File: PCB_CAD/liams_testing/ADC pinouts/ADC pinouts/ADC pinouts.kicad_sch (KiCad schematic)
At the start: 7 parts, among them U1 AK5720VT

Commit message: Changed some i2s configuation in stm32cubeMX, continued to update pinouts for the ADC
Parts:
- added J1: Conn_Coaxial_x2, symbol Connector:Conn_Coaxial_x2
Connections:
- net GND: now also J1.3 (EXT)
- net left channel in: no longer names the net of U1.3 (LIN)
- net left channel in: now also J1.2 (IN2)
- net right channel in: no longer names the net of U1.2 (RIN)
- net right channel in: now also J1.1 (IN1)
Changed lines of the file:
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@@
 		)
 	)
-	(label "right channel in"
-		(at 97.79 64.77 0)
+	(label "to ucontroller"
+		(at 144.78 64.77 0)
 		(fields_autoplaced yes)
 		(effects
@@
 	)
 	(label "to ucontroller"
-		(at 144.78 64.77 0)
+		(at 144.78 62.23 0)
 		(fields_autoplaced yes)
 		(effects
@@
 		)
 	)
-	(label "to ucontroller"
-		(at 144.78 62.23 0)
+	(label "data line to microcontroller"
+		(at 158.75 69.85 0)
 		(fields_autoplaced yes)
 		(effects
@@
 		)
 	)
-	(label "left channel in"
-		(at 97.79 69.85 0)
-		(fields_autoplaced yes)
-		(effects
-			(font
-				(size 1.27 1.27)
-			)
-			(justify left bottom)
-		)
-	)
-	(label "data line to microcontroller"
-		(at 158.75 69.85 0)
-		(fields_autoplaced yes)
-		(effects
-			(font
-				(size 1.27 1.27)
-			)
-			(justify left bottom)
+	(symbol
+		(lib_id "Connector:Conn_Coaxial_x2")
+		(at 92.71 67.31 0)
+		(mirror y)
+		(unit 1)
+		(exclude_from_sim no)
+		(in_bom yes)
+		(on_board yes)
+		(dnp no)
+		(property "Reference" "J1"
+			(at 88.9 66.3331 0)
+			(effects
+				(font
+					(size 1.27 1.27)
+				)
+				(justify left)
+			)
+		)
+		(property "Value" "Conn_Coaxial_x2"
+			(at 88.9 68.8731 0)
+			(effects
+				(font
+					(size 1.27 1.27)
+				)
+				(justify left)
+			)
+		)
+		(property "Footprint" ""
+			(at 92.71 69.85 0)
+			(effects
+				(font
+					(size 1.27 1.27)
+				)
+				(hide yes)
+			)
+		)
+		(property "Datasheet" "~"
+			(at 92.71 69.85 0)
+			(effects
+				(font
+					(size 1.27 1.27)
+				)
+				(hide yes)
+			)
+		)
+		(property "Description" "double coaxial connector (BNC, SMA, SMB, SMC, Cinch/RCA, LEMO, ...)"
+			(at 92.71 67.31 0)
+			(effects
+				(font
+					(size 1.27 1.27)
+				)
+				(hide yes)
+			)
+		)
+		(pin "1"
+		)
+		(pin "3"
+		)
+		(pin "2"
+		)
+		(instances
+			(project ""
+				(path "/6c2c704c-81e1-41a8-9c5c-820cc3db9596"
+					(reference "J1")
+					(unit 1)
+				)
+			)
 		)
 	)
@@
 					(unit 1)
 				)
+			)
+		)
+	)
+	(symbol
+		(lib_id "power:GND")
+		(at 92.71 74.93 0)
+		(unit 1)
+		(exclude_from_sim no)
+		(in_bom yes)
+		(on_board yes)
+		(dnp no)
+		(fields_autoplaced yes)
+		(property "Reference" "#PWR07"
+			(at 92.71 81.28 0)
+			(effects
+				(font
+					(size 1.27 1.27)
+				)
+				(hide yes)
+			)
+		)
+		(property "Value" "GND"
+			(at 92.71 80.01 0)
+			(effects
+				(font
+					(size 1.27 1.27)
+				)
+			)
+		)
+		(property "Footprint" ""
+			(at 92.71 74.93 0)
+			(effects
+				(font
+					(size 1.27 1.27)
+				)
+				(hide yes)
+			)
+		)
+		(property "Datasheet" ""
+			(at 92.71 74.93 0)
+			(effects
+				(font
+					(size 1.27 1.27)
+				)
+				(hide yes)
+			)
+		)
+		(property "Description" "Power symbol creates a global label with name \"GND\" , ground"
+			(at 92.71 74.93 0)
+			(effects
+				(font
+					(size 1.27 1.27)
+				)
+				(hide yes)
+			)
+		)
+		(pin "1"
+		)
+		(instances
+			(project "ADC pinouts"
+				(path "/6c2c704c-81e1-41a8-9c5c-820cc3db9596"
+					(reference "#PWR07")
+					(unit 1)
+				)

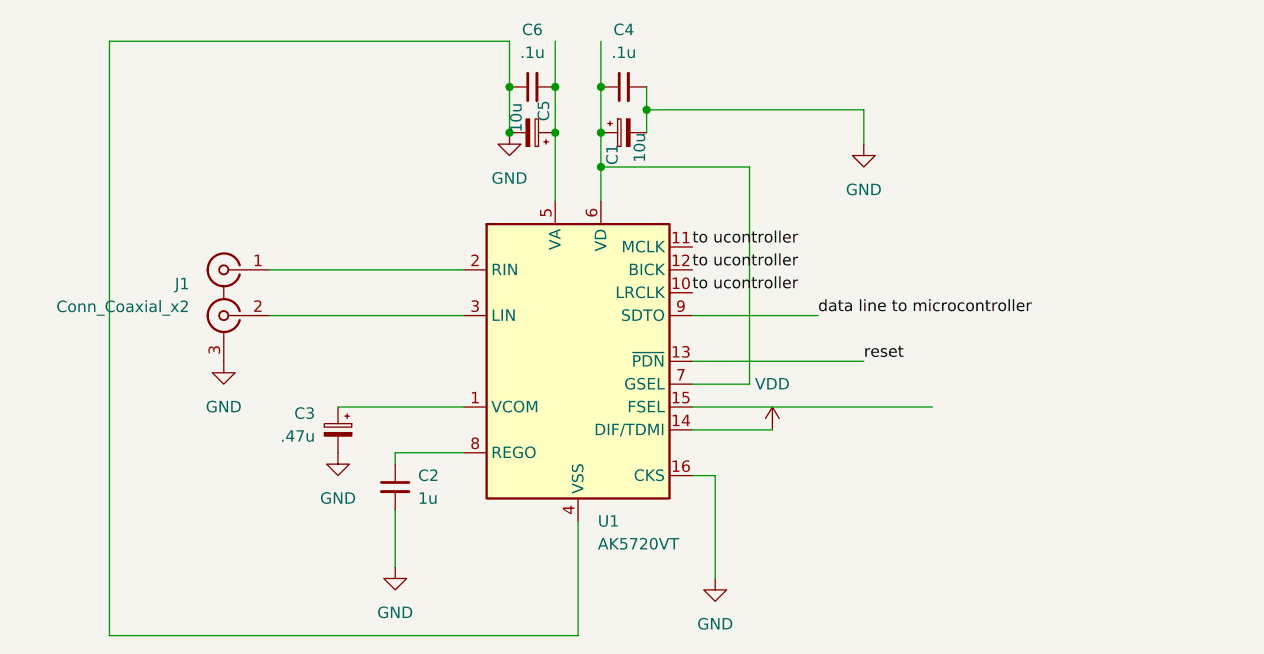
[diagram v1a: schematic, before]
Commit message: added my adc pinouts to main circuit schematic in kicad
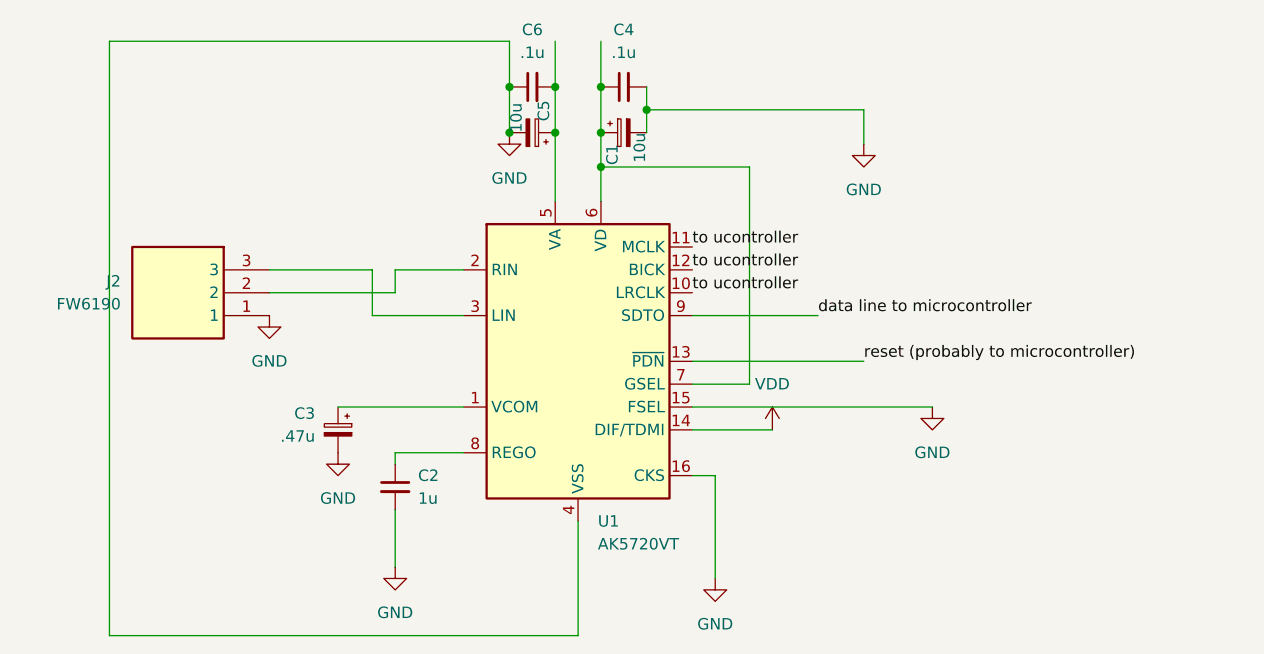
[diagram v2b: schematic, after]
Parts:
- removed J1: Conn_Coaxial_x2, symbol Connector:Conn_Coaxial_x2
- added J2: FW6190, FW6190, symbol FW6190:FW6190
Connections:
- net GND: now also U1.15 (FSEL), J2.1
- net at U1.2 (RIN): now also J2.2
- net at U1.3 (LIN): now also J2.3
- net reset renamed reset (probably to microcontroller)
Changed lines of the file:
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@@
+	(wire
+		(pts
+			(xy 111.76 64.77) (xy 111.76 67.31)
+		)
+		(stroke
+			(width 0)
+			(type default)
+		)
+	)
 	(wire
 		(pts
@@
 	(wire
 		(pts
+			(xy 109.22 64.77) (xy 97.79 64.77)
+		)
+		(stroke
+			(width 0)
+			(type default)
+		)
+	)
+	(wire
+		(pts
 			(xy 147.32 99.06) (xy 147.32 87.63)
 		)
@@
 	(wire
 		(pts
+			(xy 119.38 64.77) (xy 111.76 64.77)
+		)
+		(stroke
+			(width 0)
+			(type default)
+		)
+	)
+	(wire
+		(pts
 			(xy 144.78 69.85) (xy 158.75 69.85)
 		)
@@
 	(wire
 		(pts
+			(xy 109.22 64.77) (xy 109.22 69.85)
+		)
+		(stroke
+			(width 0)
+			(type default)
+		)
+	)
+	(wire
+		(pts
+			(xy 111.76 67.31) (xy 97.79 67.31)
+		)
+		(stroke
+			(width 0)
+			(type default)
+		)
+	)
+	(wire
+		(pts
 			(xy 111.76 91.44) (xy 111.76 97.79)
 		)
@@
 	(wire
 		(pts
+			(xy 109.22 69.85) (xy 119.38 69.85)
+		)
+		(stroke
+			(width 0)
+			(type default)
+		)
+	)
+	(wire
+		(pts
 			(xy 147.32 87.63) (xy 144.78 87.63)
 		)
@@
 	(wire
 		(pts
-			(xy 97.79 69.85) (xy 119.38 69.85)
-		)
-		(stroke
-			(width 0)
-			(type default)
-		)
-	)
-	(wire
-		(pts
 			(xy 151.13 77.47) (xy 151.13 53.34)
 		)
@@
 		(pts
 			(xy 139.7 44.45) (xy 139.7 46.99)
-		)
-		(stroke
-			(width 0)
-			(type default)
-		)
-	)
-	(wire
-		(pts
-			(xy 97.79 64.77) (xy 119.38 64.77)
 		)
 		(stroke
@@
 		)
 	)
-	(label "reset"
+	(label "reset (probably to microcontroller)"
 		(at 163.83 74.93 0)
 		(fields_autoplaced yes)
@@
 	)
 	(symbol
-		(lib_id "Connector:Conn_Coaxial_x2")
-		(at 92.71 67.31 0)
+		(lib_id "FW6190:FW6190")
+		(at 97.79 64.77 0)
 		(mirror y)
 		(unit 1)
@@
 		(on_board yes)
 		(dnp no)
-		(property "Reference" "J1"
-			(at 88.9 66.3331 0)
+		(property "Reference" "J2"
+			(at 81.28 66.0399 0)
 			(effects
 				(font
@@
 			)
 		)
-		(property "Value" "Conn_Coaxial_x2"
-			(at 88.9 68.8731 0)
+		(property "Value" "FW6190"
+			(at 81.28 68.5799 0)
 			(effects
 				(font
@@
 			)
 		)
-		(property "Footprint" ""
-			(at 92.71 69.85 0)
-			(effects
-				(font
-					(size 1.27 1.27)
-				)
-				(hide yes)
-			)
-		)
-		(property "Datasheet" "~"
-			(at 92.71 69.85 0)
-			(effects
-				(font
-					(size 1.27 1.27)
-				)
-				(hide yes)
-			)
-		)
-		(property "Description" "double coaxial connector (BNC, SMA, SMB, SMC, Cinch/RCA, LEMO, ...)"
-			(at 92.71 67.31 0)
-			(effects
-				(font
-					(size 1.27 1.27)
-				)
+		(property "Footprint" "FW6190"
+			(at 81.28 159.69 0)
+			(effects
+				(font
+					(size 1.27 1.27)
+				)
+				(justify left top)
+				(hide yes)
+			)
+		)
+		(property "Datasheet" "https://www.cliffuk.co.uk/products/phono/phonoIS.pdf"
+			(at 81.28 259.69 0)
+			(effects
+				(font
+					(size 1.27 1.27)
+				)
+				(justify left top)
+				(hide yes)
+			)
+		)
+		(property "Description" "3.20mm ID, 9.00mm OD (RCA) Phono (RCA) Jack, Dual Mono Connector Solder"
+			(at 97.79 64.77 0)
+			(effects
+				(font
+					(size 1.27 1.27)
+				)
+				(hide yes)
+			)
+		)
+		(property "Height" "20"
+			(at 81.28 459.69 0)
+			(effects
+				(font
+					(size 1.27 1.27)
+				)
+				(justify left top)
+				(hide yes)
+			)
+		)
+		(property "Manufacturer_Name" "CLIFF ELECTRONIC COMPONENTS"
+			(at 81.28 559.69 0)
+			(effects
+				(font
+					(size 1.27 1.27)
+				)
+				(justify left top)
+				(hide yes)
+			)
+		)
+		(property "Manufacturer_Part_Number" "FW6190"
+			(at 81.28 659.69 0)
+			(effects
+				(font
+					(size 1.27 1.27)
+				)
+				(justify left top)
+				(hide yes)
+			)
+		)
+		(property "Mouser Part Number" ""
+			(at 81.28 759.69 0)
+			(effects
+				(font
+					(size 1.27 1.27)
+				)
+				(justify left top)
+				(hide yes)
+			)
+		)
+		(property "Mouser Price/Stock" ""
+			(at 81.28 859.69 0)
+			(effects
+				(font
+					(size 1.27 1.27)
+				)
+				(justify left top)
+				(hide yes)
+			)
+		)
+		(property "Arrow Part Number" ""
+			(at 81.28 959.69 0)
+			(effects
+				(font
+					(size 1.27 1.27)
+				)
+				(justify left top)
+				(hide yes)
+			)
+		)
+		(property "Arrow Price/Stock" ""
+			(at 81.28 1059.69 0)
+			(effects
+				(font
+					(size 1.27 1.27)
+				)
+				(justify left top)
 				(hide yes)
 			)
@@
 		(pin "1"
 		)
+		(pin "2"
+		)
 		(pin "3"
-		)
-		(pin "2"
 		)
 		(instances
 			(project ""
 				(path "/6c2c704c-81e1-41a8-9c5c-820cc3db9596"
-					(reference "J1")
+					(reference "J2")
 					(unit 1)
 				)
@@
 	(symbol
 		(lib_id "power:GND")
-		(at 92.71 74.93 0)
+		(at 97.79 69.85 0)
 		(unit 1)
 		(exclude_from_sim no)
@@
 		(fields_autoplaced yes)
 		(property "Reference" "#PWR07"
-			(at 92.71 81.28 0)
+			(at 97.79 76.2 0)
 			(effects
 				(font
@@
 		)
 		(property "Value" "GND"
-			(at 92.71 80.01 0)
+			(at 97.79 74.93 0)
 			(effects
 				(font
@@
 		)
 		(property "Footprint" ""
-			(at 92.71 74.93 0)
+			(at 97.79 69.85 0)
 			(effects
 				(font
@@
 		)
 		(property "Datasheet" ""
-			(at 92.71 74.93 0)
+			(at 97.79 69.85 0)
 			(effects
 				(font
@@
 		)
 		(property "Description" "Power symbol creates a global label with name \"GND\" , ground"
-			(at 92.71 74.93 0)
+			(at 97.79 69.85 0)
 			(effects
 				(font
@@
 					(unit 1)
 				)
+			)
+		)
+	)
+	(symbol
+		(lib_id "power:GND")
+		(at 171.45 80.01 0)
+		(unit 1)
+		(exclude_from_sim no)
+		(in_bom yes)
+		(on_board yes)
+		(dnp no)
+		(fields_autoplaced yes)
+		(property "Reference" "#PWR08"
+			(at 171.45 86.36 0)
+			(effects
+				(font
+					(size 1.27 1.27)
+				)
+				(hide yes)
+			)
+		)
+		(property "Value" "GND"
+			(at 171.45 85.09 0)
+			(effects
+				(font
+					(size 1.27 1.27)
+				)
+			)
+		)
+		(property "Footprint" ""
+			(at 171.45 80.01 0)
+			(effects
+				(font
+					(size 1.27 1.27)
+				)
+				(hide yes)
+			)
+		)
+		(property "Datasheet" ""
+			(at 171.45 80.01 0)
+			(effects
+				(font
+					(size 1.27 1.27)
+				)
+				(hide yes)
+			)
+		)
+		(property "Description" "Power symbol creates a global label with name \"GND\" , ground"
+			(at 171.45 80.01 0)
+			(effects
+				(font
+					(size 1.27 1.27)
+				)
+				(hide yes)
+			)
+		)
+		(pin "1"
+		)
+		(instances
+			(project ""
+				(path "/6c2c704c-81e1-41a8-9c5c-820cc3db9596"
+					(reference "#PWR08")
+					(unit 1)
+				)
